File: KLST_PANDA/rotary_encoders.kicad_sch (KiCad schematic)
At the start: 0 parts

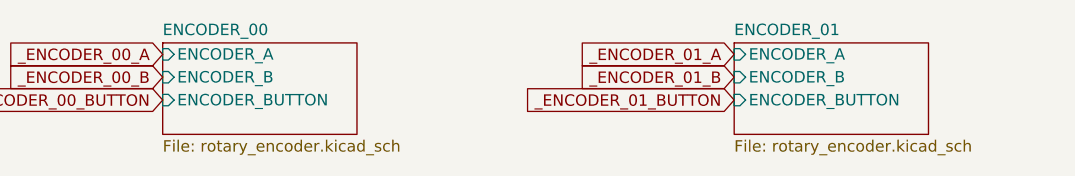
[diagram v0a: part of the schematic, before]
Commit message: added IDC, updated pin names
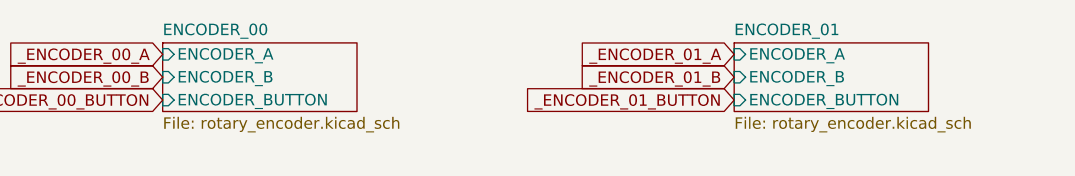
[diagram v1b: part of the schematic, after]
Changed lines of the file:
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@@
     )
   )
-  (sheet (at 111.76 93.98) (size 21.59 10.16) (fields_autoplaced)
+  (sheet (at 111.76 93.98) (size 21.59 7.62) (fields_autoplaced)
     (stroke (width 0.1524) (type solid))
     (fill (color 0 0 0 0.0000))
@@
       (effects (font (size 1.27 1.27)) (justify left bottom))
     )
-    (property "Sheetfile" "rotary_encoder.kicad_sch" (at 111.76 104.7246 0)
+    (property "Sheetfile" "rotary_encoder.kicad_sch" (at 111.76 102.1846 0)
       (effects (font (size 1.27 1.27)) (justify left top))
     )
@@
     )
   )
-  (sheet (at 175.26 93.98) (size 21.59 10.16) (fields_autoplaced)
+  (sheet (at 175.26 93.98) (size 21.59 7.62) (fields_autoplaced)
     (stroke (width 0.1524) (type solid))
     (fill (color 0 0 0 0.0000))
@@
       (effects (font (size 1.27 1.27)) (justify left bottom))
     )
-    (property "Sheetfile" "rotary_encoder.kicad_sch" (at 175.26 104.7246 0)
+    (property "Sheetfile" "rotary_encoder.kicad_sch" (at 175.26 102.1846 0)
       (effects (font (size 1.27 1.27)) (justify left top))
     )

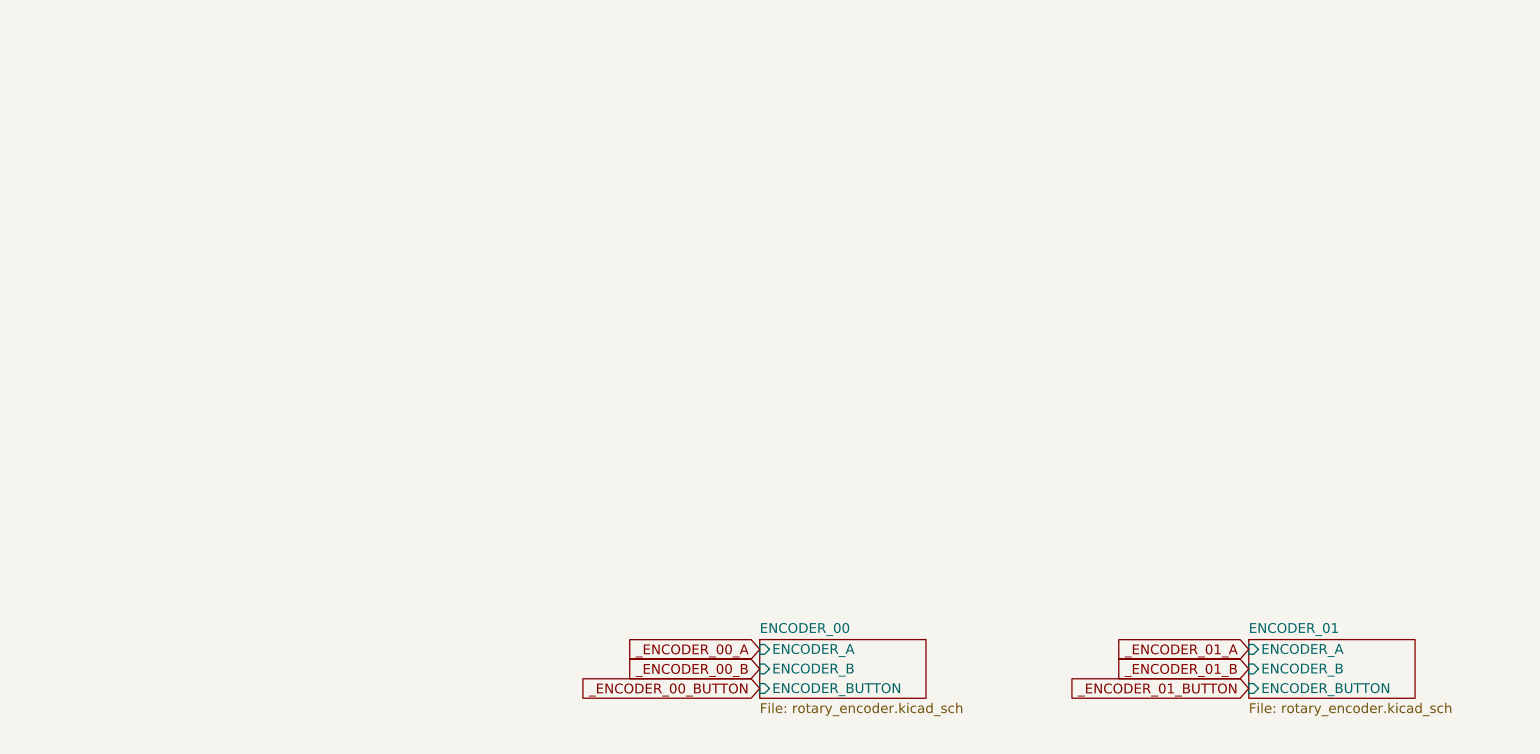
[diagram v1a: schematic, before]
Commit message: moved core (MCU) to sheet, cleaned up sheets
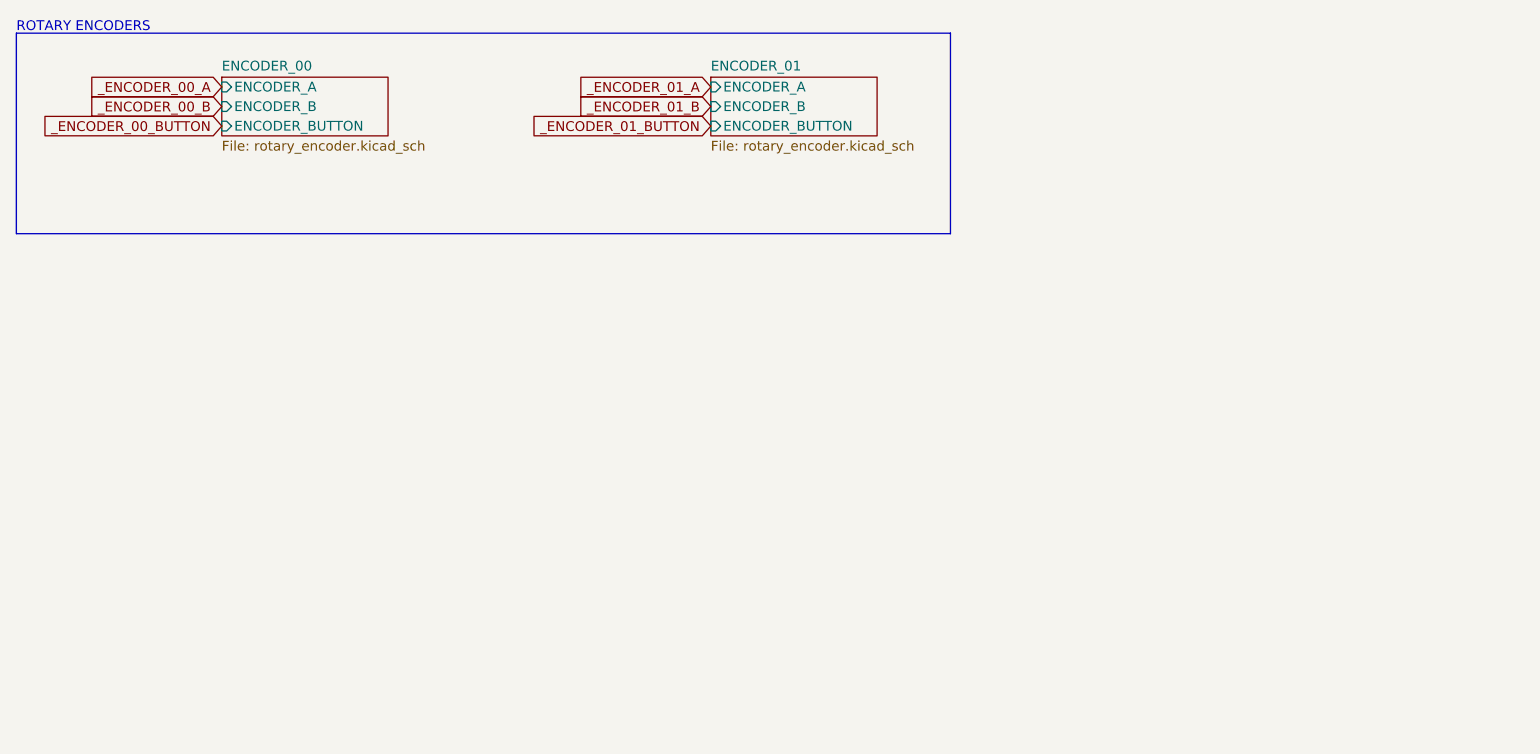
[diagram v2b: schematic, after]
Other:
- note added: "ROTARY ENCODERS"
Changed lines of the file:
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@@
 (kicad_sch (version 20230121) (generator eeschema)
   (paper "A4")
-  (global_label "_ENCODER_01_B" (shape input) (at 175.26 97.79 180) (fields_autoplaced)
+  (rectangle (start 15.24 15.24) (end 136.525 41.275)
+    (stroke (width 0) (type default))
+    (fill (type none))
+  )
+  (text "ROTARY ENCODERS" (at 15.24 15.24 0)
+    (effects (font (size 1.27 1.27)) (justify left bottom))
+  )
+  (global_label "_ENCODER_01_B" (shape input) (at 105.41 24.765 180) (fields_autoplaced)
     (effects (font (size 1.27 1.27)) (justify right))
-    (property "Intersheetrefs" "${INTERSHEET_REFS}" (at 156.9934 97.79 0)
+    (property "Intersheetrefs" "${INTERSHEET_REFS}" (at 87.1434 24.765 0)
       (effects (font (size 1.27 1.27)) (justify right) hide)
     )
   )
-  (global_label "_ENCODER_00_A" (shape input) (at 111.76 95.25 180) (fields_autoplaced)
+  (global_label "_ENCODER_00_A" (shape input) (at 41.91 22.225 180) (fields_autoplaced)
     (effects (font (size 1.27 1.27)) (justify right))
-    (property "Intersheetrefs" "${INTERSHEET_REFS}" (at 93.6748 95.25 0)
+    (property "Intersheetrefs" "${INTERSHEET_REFS}" (at 23.8248 22.225 0)
       (effects (font (size 1.27 1.27)) (justify right) hide)
     )
   )
-  (global_label "_ENCODER_01_BUTTON" (shape input) (at 175.26 100.33 180) (fields_autoplaced)
+  (global_label "_ENCODER_01_BUTTON" (shape input) (at 105.41 27.305 180) (fields_autoplaced)
     (effects (font (size 1.27 1.27)) (justify right))
-    (property "Intersheetrefs" "${INTERSHEET_REFS}" (at 151.0667 100.33 0)
+    (property "Intersheetrefs" "${INTERSHEET_REFS}" (at 81.2167 27.305 0)
       (effects (font (size 1.27 1.27)) (justify right) hide)
     )
   )
-  (global_label "_ENCODER_00_B" (shape input) (at 111.76 97.79 180) (fields_autoplaced)
+  (global_label "_ENCODER_00_B" (shape input) (at 41.91 24.765 180) (fields_autoplaced)
     (effects (font (size 1.27 1.27)) (justify right))
-    (property "Intersheetrefs" "${INTERSHEET_REFS}" (at 93.4934 97.79 0)
+    (property "Intersheetrefs" "${INTERSHEET_REFS}" (at 23.6434 24.765 0)
       (effects (font (size 1.27 1.27)) (justify right) hide)
     )
   )
-  (global_label "_ENCODER_00_BUTTON" (shape input) (at 111.76 100.33 180) (fields_autoplaced)
+  (global_label "_ENCODER_00_BUTTON" (shape input) (at 41.91 27.305 180) (fields_autoplaced)
     (effects (font (size 1.27 1.27)) (justify right))
-    (property "Intersheetrefs" "${INTERSHEET_REFS}" (at 87.5667 100.33 0)
+    (property "Intersheetrefs" "${INTERSHEET_REFS}" (at 17.7167 27.305 0)
       (effects (font (size 1.27 1.27)) (justify right) hide)
     )
   )
-  (global_label "_ENCODER_01_A" (shape input) (at 175.26 95.25 180) (fields_autoplaced)
+  (global_label "_ENCODER_01_A" (shape input) (at 105.41 22.225 180) (fields_autoplaced)
     (effects (font (size 1.27 1.27)) (justify right))
-    (property "Intersheetrefs" "${INTERSHEET_REFS}" (at 157.1748 95.25 0)
+    (property "Intersheetrefs" "${INTERSHEET_REFS}" (at 87.3248 22.225 0)
       (effects (font (size 1.27 1.27)) (justify right) hide)
     )
   )
-  (sheet (at 111.76 93.98) (size 21.59 7.62) (fields_autoplaced)
+  (sheet (at 41.91 20.955) (size 21.59 7.62) (fields_autoplaced)
     (stroke (width 0.1524) (type solid))
     (fill (color 0 0 0 0.0000))
-    (property "Sheetname" "ENCODER_00" (at 111.76 93.2684 0)
+    (property "Sheetname" "ENCODER_00" (at 41.91 20.2434 0)
       (effects (font (size 1.27 1.27)) (justify left bottom))
     )
-    (property "Sheetfile" "rotary_encoder.kicad_sch" (at 111.76 102.1846 0)
+    (property "Sheetfile" "rotary_encoder.kicad_sch" (at 41.91 29.1596 0)
       (effects (font (size 1.27 1.27)) (justify left top))
     )
-    (pin "ENCODER_B" input (at 111.76 97.79 180)
+    (pin "ENCODER_B" input (at 41.91 24.765 180)
       (effects (font (size 1.27 1.27)) (justify left))
     )
-    (pin "ENCODER_BUTTON" input (at 111.76 100.33 180)
+    (pin "ENCODER_BUTTON" input (at 41.91 27.305 180)
       (effects (font (size 1.27 1.27)) (justify left))
     )
-    (pin "ENCODER_A" input (at 111.76 95.25 180)
+    (pin "ENCODER_A" input (at 41.91 22.225 180)
       (effects (font (size 1.27 1.27)) (justify left))
     )
@@
     )
   )
-  (sheet (at 175.26 93.98) (size 21.59 7.62) (fields_autoplaced)
+  (sheet (at 105.41 20.955) (size 21.59 7.62) (fields_autoplaced)
     (stroke (width 0.1524) (type solid))
     (fill (color 0 0 0 0.0000))
-    (property "Sheetname" "ENCODER_01" (at 175.26 93.2684 0)
+    (property "Sheetname" "ENCODER_01" (at 105.41 20.2434 0)
       (effects (font (size 1.27 1.27)) (justify left bottom))
     )
-    (property "Sheetfile" "rotary_encoder.kicad_sch" (at 175.26 102.1846 0)
+    (property "Sheetfile" "rotary_encoder.kicad_sch" (at 105.41 29.1596 0)
       (effects (font (size 1.27 1.27)) (justify left top))
     )
-    (pin "ENCODER_B" input (at 175.26 97.79 180)
+    (pin "ENCODER_B" input (at 105.41 24.765 180)
       (effects (font (size 1.27 1.27)) (justify left))
     )
-    (pin "ENCODER_BUTTON" input (at 175.26 100.33 180)
+    (pin "ENCODER_BUTTON" input (at 105.41 27.305 180)
       (effects (font (size 1.27 1.27)) (justify left))
     )
-    (pin "ENCODER_A" input (at 175.26 95.25 180)
+    (pin "ENCODER_A" input (at 105.41 22.225 180)
       (effects (font (size 1.27 1.27)) (justify left))
     )
